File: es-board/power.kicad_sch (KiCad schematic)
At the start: 29 parts, among them J2 USB_C_Receptacle_USB2.0, Q1 Q_PMOS_GSD, Q2 Q_PMOS_GSD, U1 IP4234CZ6,125, U3 CYPD3177, U4 IFX25001TFV50ATMA1

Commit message: Updated footprints
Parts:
- C13, C14: footprint (none) -> Capacitor_SMD:C_1206_3216Metric
- D5: footprint (none) -> Diode_SMD:D_1206_3216Metric
- R10, R11: footprint (none) -> Resistor_SMD:R_1206_3216Metric
- R4, R5: footprint Resistor_SMD:R_0603_1608Metric -> Resistor_SMD:R_1206_3216Metric
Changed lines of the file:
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@@
       (effects (font (size 1.27 1.27)))
     )
-    (property "Footprint" "Resistor_SMD:R_0603_1608Metric" (at 88.9 73.152 90)
+    (property "Footprint" "Resistor_SMD:R_1206_3216Metric" (at 88.9 73.152 90)
       (effects (font (size 1.27 1.27)) hide)
     )
@@
       (effects (font (size 1.27 1.27)))
     )
-    (property "Footprint" "Resistor_SMD:R_0603_1608Metric" (at 88.9 74.168 90)
+    (property "Footprint" "Resistor_SMD:R_1206_3216Metric" (at 88.9 74.168 90)
       (effects (font (size 1.27 1.27)) hide)
     )
@@
       (effects (font (size 1.27 1.27)) (justify left))
     )
-    (property "Footprint" "" (at 215.392 41.91 90)
+    (property "Footprint" "Resistor_SMD:R_1206_3216Metric" (at 215.392 41.91 90)
       (effects (font (size 1.27 1.27)) hide)
     )
@@
       (effects (font (size 1.27 1.27)))
     )
-    (property "Footprint" "" (at 81.28 137.16 0)
+    (property "Footprint" "Diode_SMD:D_1206_3216Metric" (at 81.28 137.16 0)
       (effects (font (size 1.27 1.27)) hide)
     )
@@
       (effects (font (size 1.27 1.27)) (justify right))
     )
-    (property "Footprint" "" (at 72.6948 140.97 0)
+    (property "Footprint" "Capacitor_SMD:C_1206_3216Metric" (at 72.6948 140.97 0)
       (effects (font (size 1.27 1.27)) hide)
     )
@@
       (effects (font (size 1.27 1.27)) (justify left))
     )
-    (property "Footprint" "" (at 91.1352 148.59 0)
+    (property "Footprint" "Capacitor_SMD:C_1206_3216Metric" (at 91.1352 148.59 0)
       (effects (font (size 1.27 1.27)) hide)
     )
@@
       (effects (font (size 1.27 1.27)) (justify left))
     )
-    (property "Footprint" "" (at 215.392 53.34 90)
-      (effects (font (size 1.27 1.27)) hide)
-    )
+    (property "Footprint" "Resistor_SMD:R_1206_3216Metric" (at 215.392 53.34 90)
+      (effects (font (size 1.27 1.27)) hide)
+    )

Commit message: Added BOM
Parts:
- C10: value 10u -> 10u 50V; DPN 1276-1097-1-ND -> 1276-6736-1-ND; DPN-m 187-CL31A106MBHNNNE -> (none); MPN CL31B105KAHNNNE -> CAP CER 10UF 50V X5R 1206; MPN-m CL31A106MBHNNNE -> (none)
- C11, C12: DPN 1276-1097-1-ND -> 1276-3091-1-ND; DPN-m 187-CL31B105KBHNFNE -> (none); MPN CL31B105KAHNNNE -> CL31B105KBHNFNE; MPN-m CL31B105KBHNFNE -> (none)
- C13: DPN (none) -> 1276-2728-1-ND; MPN (none) -> CL31A226MOCLNNC
- C14: DPN (none) -> 490-GRM31CR61A107MEA8LCT-ND; MPN (none) -> GRM31CR61A107MEA8L
- C8: value 10u -> 10u 50V; DPN 1276-1075-1-ND -> 1276-6736-1-ND; DPN-m 187-CL31A106MBHNNNE -> (none); MPN CL31A106KAHNNNE -> CAP CER 10UF 50V X5R 1206; MPN-m CL31A106MBHNNNE -> (none)
- C9: value 1u -> 1u 50V; DPN 1276-1097-1-ND -> 1276-3091-1-ND; DPN-m 187-CL31B105KBHNFNE -> (none); MPN CL31B105KAHNNNE -> CL31B105KBHNFNE; MPN-m CL31B105KBHNFNE -> (none)
- D3: value LED -> red; DPN 160-1169-1-ND -> 160-1168-1-ND; DPN-m 710-156120RS75000 -> (none); MPN LTST-C150GKT -> LTST-C150EKT; MPN-m 156120RS75000 -> (none)
- D4: value LED -> green; DPN-m 710-156120RS75000 -> (none); MPN-m 156120RS75000 -> (none)
- D5: DPN (none) -> 478-7809-1-ND; MPN (none) -> SD1206T040S1R0
- F1: DPN (none) -> F3486CT-ND; DPN-m 576-1812L150/24MR -> (none); MPN (none) -> 1812L110/33MR; MPN-m 1812L150/24MR -> (none)
- J2: DPN (none) -> 2073-USB4105-GF-ACT-ND; MPN (none) -> USB4105-GF-A
- Q1, Q2: DPN (none) -> DMP3099L-7DICT-ND; DPN-m 621-DMP3099L-7 -> (none); MPN (none) -> DMP3099L-7; MPN-m DMP3099L-7 -> (none)
- R10: DPN (none) -> RMCF1206JT1K00CT-ND; MPN (none) -> RMCF1206JT1K00
- R11: value 50k -> 51k; DPN (none) -> RMCF1206JT51K0CT-ND; MPN (none) -> RMCF1206JT51K0
- R12, R13: DPN (none) -> RMCF1206JT5K10CT-ND; DPN-m 652-CR1206FX-5101ELF -> (none); MPN (none) -> RMCF1206JT5K10; MPN-m CR1206FX-5101ELF -> (none)
- R17: DPN (none) -> RMCF1206JT2K20CT-ND; DPN-m 652-CR1206FX-2201ELF -> (none); MPN (none) -> RMCF1206JT2K20; MPN-m CR1206-FX-2201ELF -> (none)
- R2: DPN (none) -> 738-RMCF1206JG10K0CT-ND; DPN-m 652-CR1206FX-1002ELF -> (none); MPN (none) -> RMCF1206JG10K0; MPN-m CR1206-FX-1002ELF -> (none)
- R3: DPN-m 652-CR1206FX-1000ELF -> (none); MPN-m CR1206-FX-1000ELF -> (none)
- R4, R5: DPN (none) -> RMCF1206JT22R0CT-ND; MPN (none) -> RMCF1206JT22R0
- R9: DPN-m 652-CR1206FX-2201ELF -> (none); MPN-m CR1206-FX-2201ELF -> (none)
- U1: DPN (none) -> 1727-4717-1-ND; MPN (none) -> IP4234CZ6,125
- U3: DPN (none) -> 448-CYPD3177-24LQXQTCT-ND; DPN-m 727-CYPD3177-24LQXQT -> (none); MPN-m CYPD3177-24LQXQT -> (none)
- U4: DPN (none) -> IFX25001TFV50ATMA1CT-ND; MPN (none) -> IFX25001TFV50ATMA1

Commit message: Finished electricaling
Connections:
- net GND: now also C13.1, C14.2, U4.2 (GND)
- net VBUS: no longer C13.1, C14.2, U4.2 (GND)
- net vbus_fused: now reaches C8.1, C9.1, F1.2, Q1.3 (D), Q1.3 (D), R11.1, R2.1, U3.18 (VBUS_IN)
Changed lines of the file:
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@@
   (junction (at 270.51 59.69) (diameter 0) (color 0 0 0 0)
   )
-  (junction (at 44.45 137.16) (diameter 0) (color 0 0 0 0)
-  )
   (junction (at 208.28 59.69) (diameter 0) (color 0 0 0 0)
-  )
-  (junction (at 59.69 151.13) (diameter 0) (color 0 0 0 0)
   )
   (junction (at 234.95 74.93) (diameter 0) (color 0 0 0 0)
@@
     (stroke (width 0) (type default))
   )
-  (wire (pts (xy 44.45 137.16) (xy 44.45 151.13))
-    (stroke (width 0) (type default))
-  )
   (wire (pts (xy 179.07 115.57) (xy 171.45 115.57))
     (stroke (width 0) (type default))
@@
     (stroke (width 0) (type default))
   )
-  (wire (pts (xy 44.45 151.13) (xy 59.69 151.13))
-    (stroke (width 0) (type default))
-  )
   (wire (pts (xy 72.39 63.5) (xy 72.39 66.04))
     (stroke (width 0) (type default))
@@
     (stroke (width 0) (type default))
   )
-  (rectangle (start 36.83 118.11) (end 105.41 156.21)
+  (rectangle (start 36.83 119.38) (end 105.41 157.48)
     (stroke (width 0) (type default))
     (fill (type none))
@@
   )
   (text "CC1" (at 114.3 63.5 0)
+    (effects (font (size 1.27 1.27)) (justify left bottom))
+  )
+  (label "vbus_fused" (at 180.34 59.69 0) (fields_autoplaced)
     (effects (font (size 1.27 1.27)) (justify left bottom))
   )
@@
         )
       )
+    )
+  )
+  (symbol (lib_id "power:GND") (at 73.66 151.13 0) (unit 1)
+    (in_bom yes) (on_board yes) (dnp no) (fields_autoplaced)
+    (property "Reference" "#PWR037" (at 73.66 157.48 0)
+      (effects (font (size 1.27 1.27)) hide)
+    )
+    (property "Value" "GND" (at 73.66 155.2631 0)
+      (effects (font (size 1.27 1.27)))
+    )
+    (property "Footprint" "" (at 73.66 151.13 0)
+      (effects (font (size 1.27 1.27)) hide)
+    )
+    (property "Datasheet" "" (at 73.66 151.13 0)
+      (effects (font (size 1.27 1.27)) hide)
+    )
+    (pin "1")
+    (instances
+      (project "es-board"
+        (path "/c2264f68-a6c3-4f6f-b950-c32c683bb958/407c9689-8177-4576-a2e4-d1338919e5f7"
+          (reference "#PWR037") (unit 1)
+        )
+      )

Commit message: updated BOM
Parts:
- C10, C8: MPN CAP CER 10UF 50V X5R 1206 -> CL31A106MBHNNNE
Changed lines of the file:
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@@
   (title_block
     (title "ExploSnake")
-    (date "2023-10-19")
-    (rev "r1")
+    (date "2023-11-15")
+    (rev "r1.0")
     (company "Team 2")
   )
@@
       (effects (font (size 1.27 1.27)) hide)
     )
-    (property "MPN" "CAP CER 10UF 50V X5R 1206" (at 270.51 67.31 0)
+    (property "MPN" "CL31A106MBHNNNE" (at 270.51 67.31 0)
       (effects (font (size 1.27 1.27)) hide)
     )
@@
       (effects (font (size 1.27 1.27)) hide)
     )
-    (property "MPN" "CAP CER 10UF 50V X5R 1206" (at 162.56 66.04 0)
-      (effects (font (size 1.27 1.27)) hide)
-    )
+    (property "MPN" "CL31A106MBHNNNE" (at 162.56 66.04 0)
+      (effects (font (size 1.27 1.27)) hide)
+    )

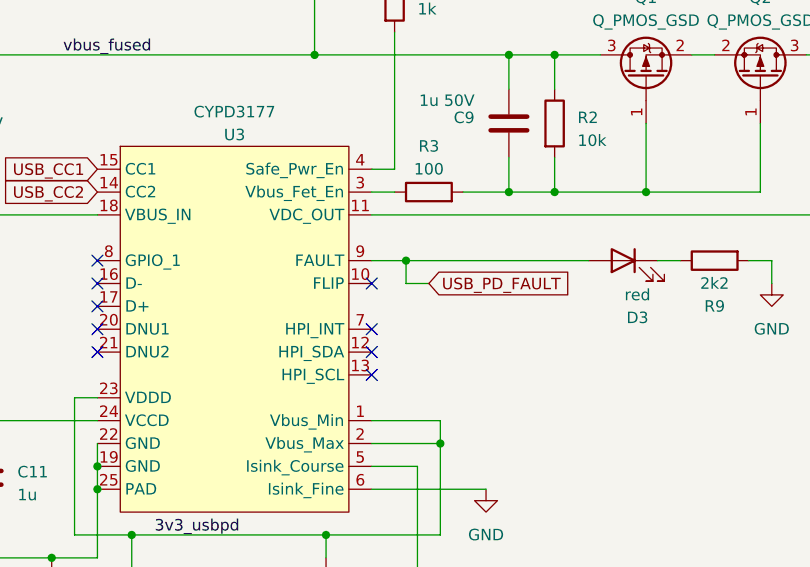
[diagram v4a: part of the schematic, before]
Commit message: Added test plan
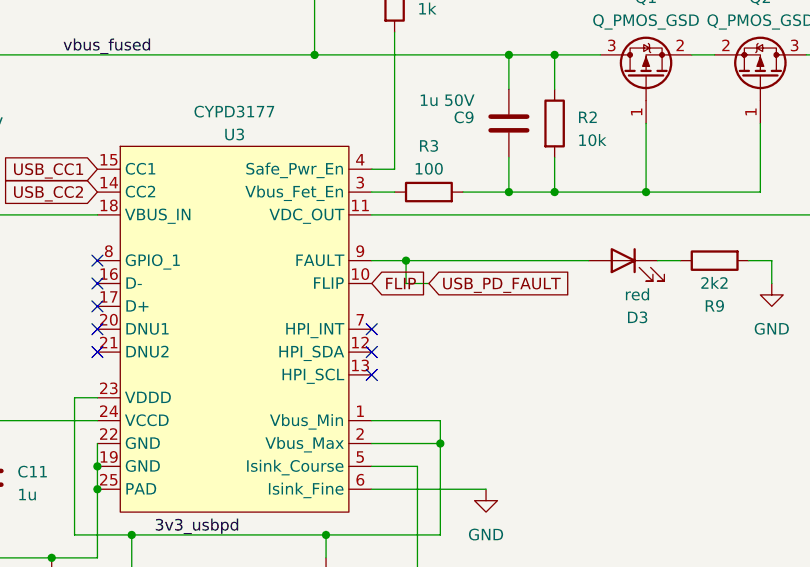
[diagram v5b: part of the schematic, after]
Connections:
- net FLIP: now reaches U3.10 (FLIP)
- no-connect marks 12 -> 11
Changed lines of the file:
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@@
   (no_connect (at 184.15 90.17))
   (no_connect (at 48.26 90.17))
-  (no_connect (at 214.63 85.09))
   (wire (pts (xy 214.63 77.47) (xy 265.43 77.47))
     (stroke (width 0) (type default))
@@
     )
   )
+  (global_label "FLIP" (shape input) (at 214.63 85.09 0) (fields_autoplaced)
+    (effects (font (size 1.27 1.27)) (justify left))
+    (property "Intersheetrefs" "${INTERSHEET_REFS}" (at 221.6067 85.09 0)
+      (effects (font (size 1.27 1.27)) (justify left) hide)
+    )
+  )
